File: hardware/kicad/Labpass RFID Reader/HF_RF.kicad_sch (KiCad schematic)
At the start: 22 parts, among them J1 Conn_01x03_Male, U4 MFRC522, Y1 27.12 MHz

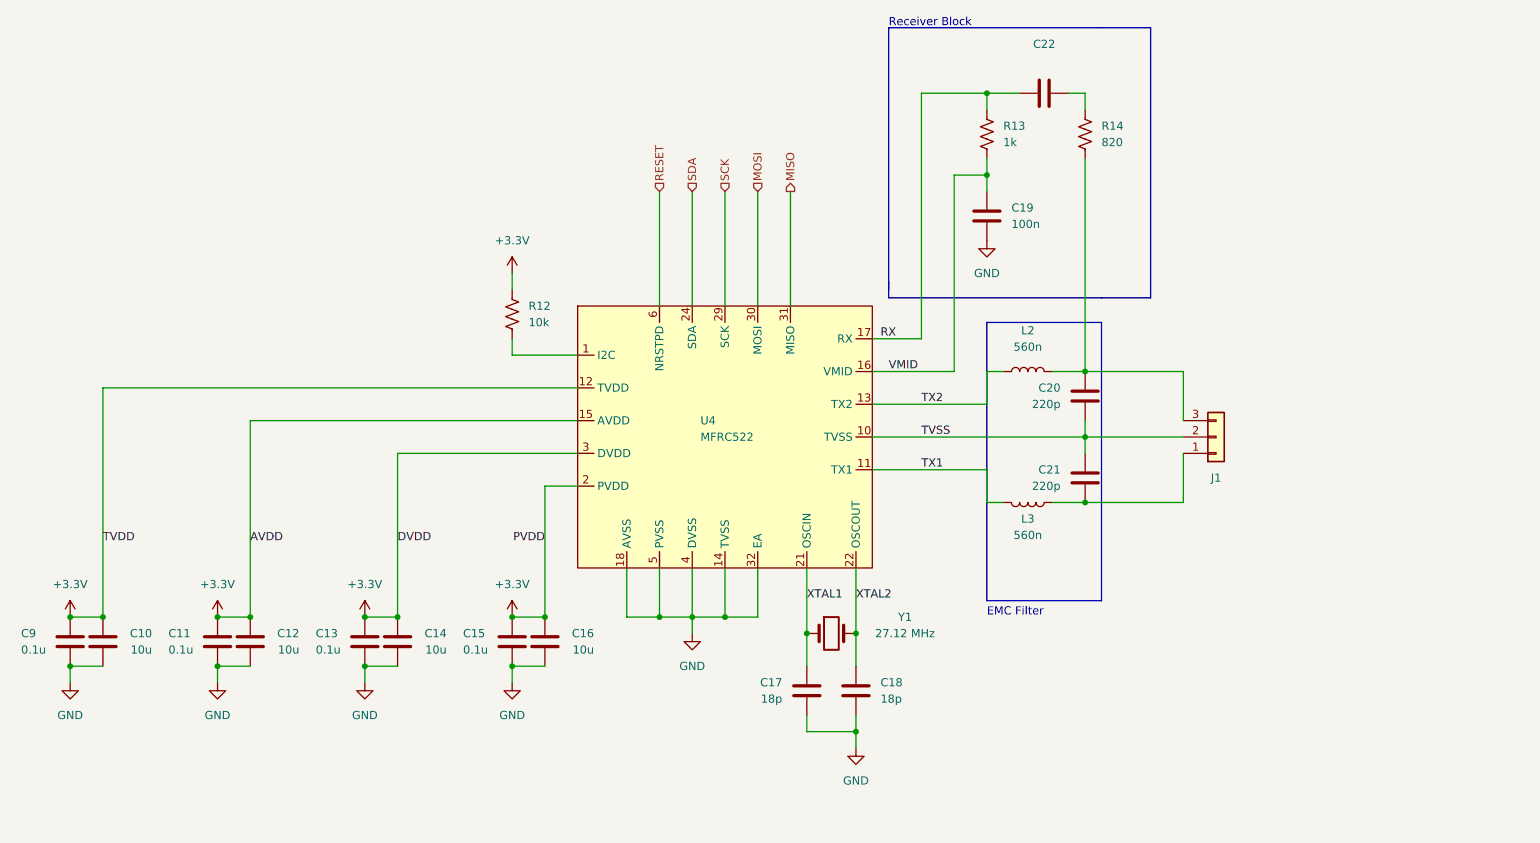
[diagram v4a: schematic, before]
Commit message: Several fixes
* EA and I2C were backwards
* Adding missing Crx into HF receive path
* Better header size and placement
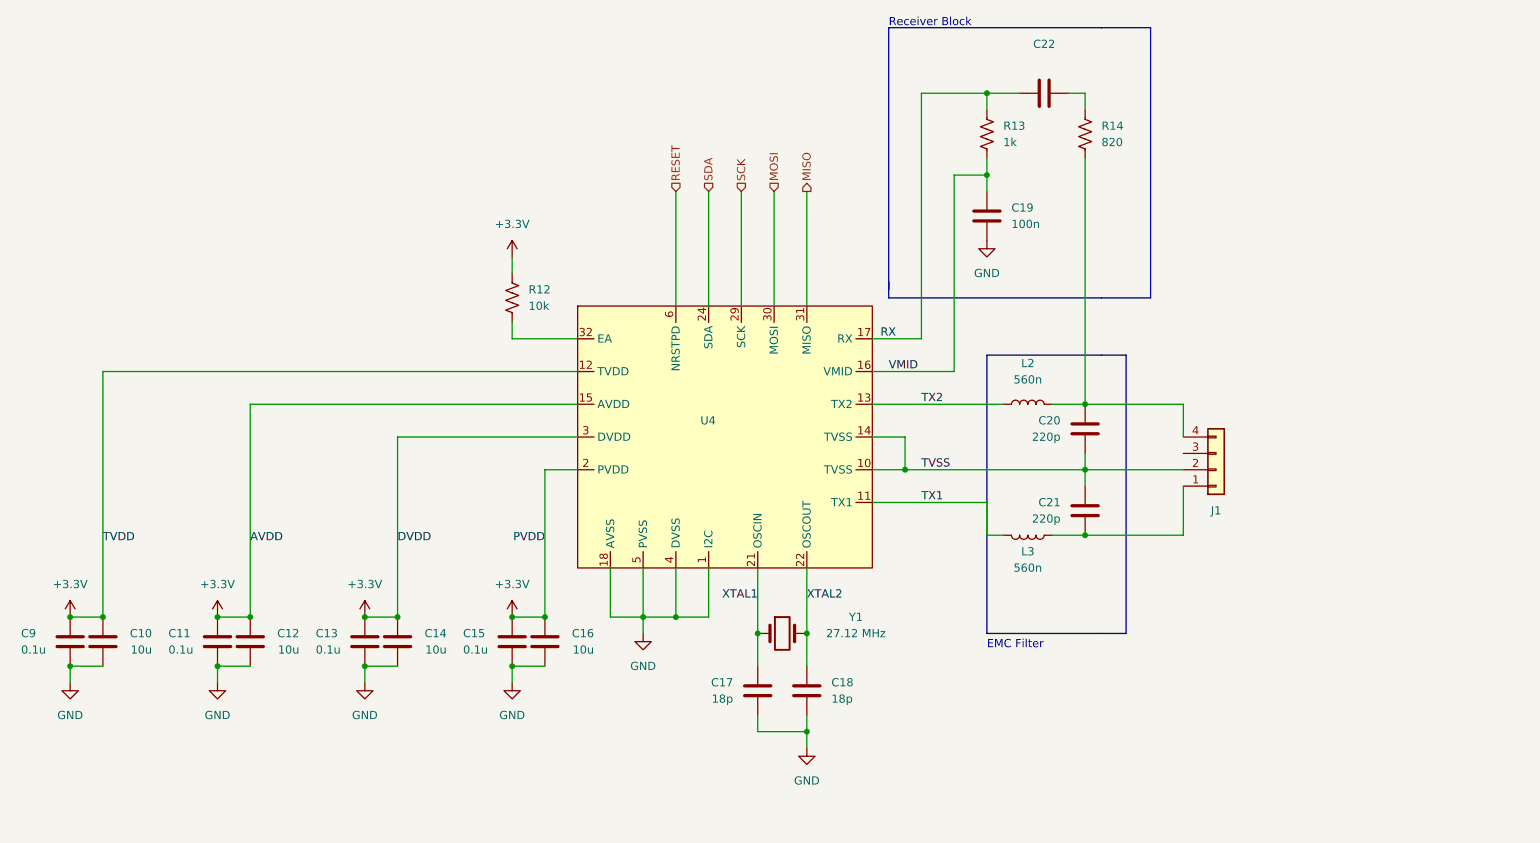
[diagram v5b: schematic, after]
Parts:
- J1: value Conn_01x03_Male -> (none); footprint Connector_PinHeader_2.54mm:PinHeader_1x03_P2.54mm_Vertical_SMD_Pin1Left -> (none); symbol Connector_Generic:Conn_01x03 -> Connector_Generic:Conn_01x04
- U4: value MFRC522 -> (none); footprint Package_QFP:LQFP-32_5x5mm_P0.5mm -> (none)
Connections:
- net GND: now also U4.1 (I2C); no longer U4.14 (TVSS), U4.32 (EA)
- net TVSS: now also U4.14 (TVSS)
- net at R12.2: now also U4.32 (EA); no longer U4.1 (I2C)
- net at C20.2, L2.2, R14.1: now also J1.4 (Pin_4); no longer J1.3 (Pin_3)
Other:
- moved on the sheet: C17, C18, C20, C21, L2, L3, R12, Y1

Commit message: Additional Changes
* remove transistor on LF path and power coil directly
  from ESP TX pin at 3.3V
* add some test points around the HF path
* add some cheap pots on LF for tuning the amplifier bias
  and comparator threshold
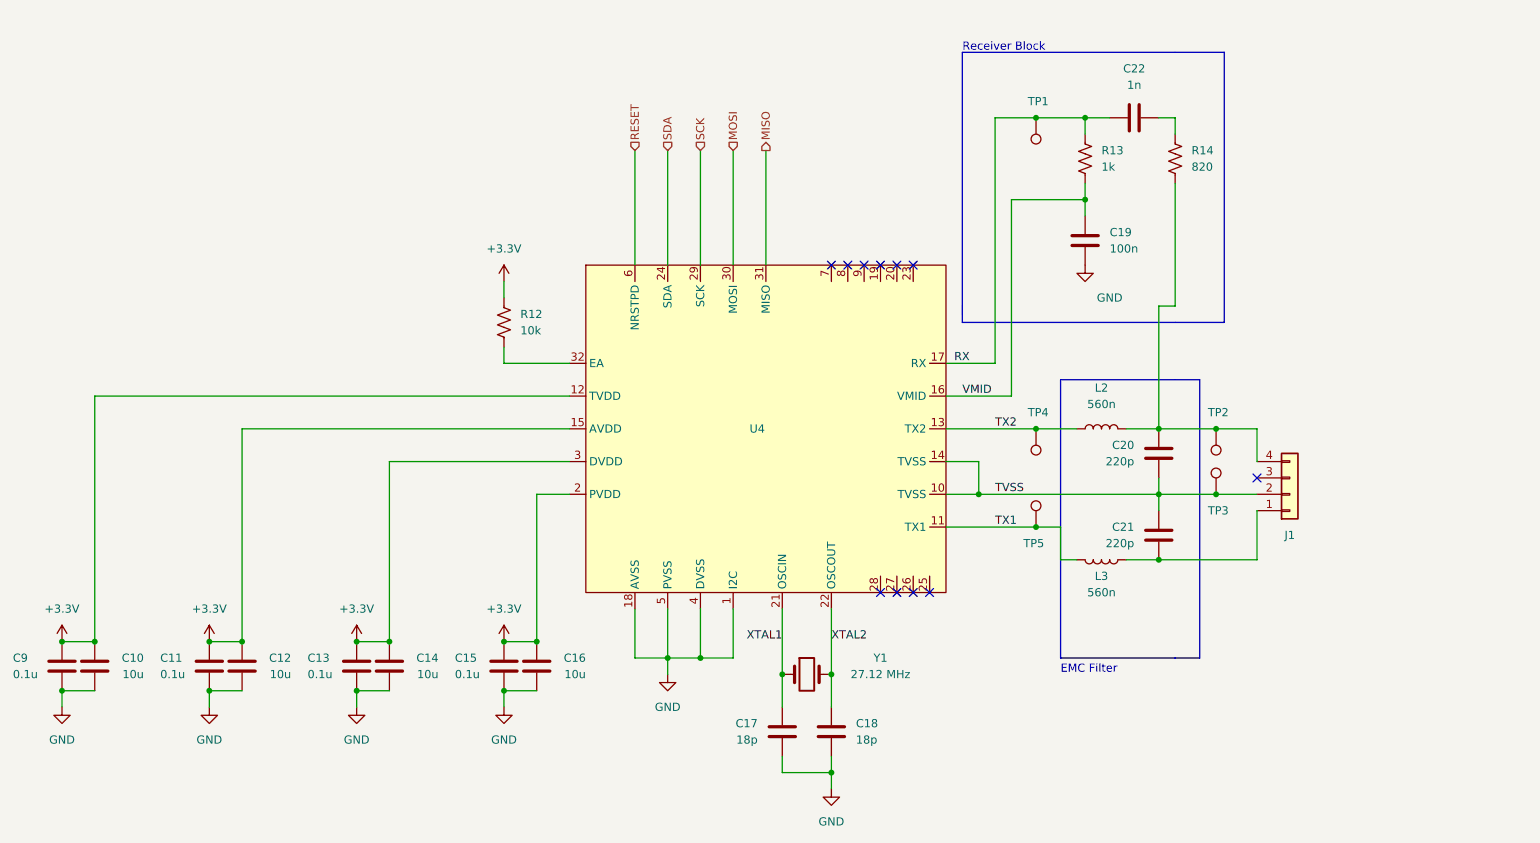
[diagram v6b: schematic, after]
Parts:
- added TP1, TP2, TP3, TP4, TP5: TestPoint, TestPoint:TestPoint_Pad_1.0x1.0mm, symbol Connector:TestPoint
- C22: value (none) -> 1n; footprint (none) -> Capacitor_SMD:C_0603_1608Metric
- J1: value (none) -> Conn_01x03_Male; footprint (none) -> Connector_PinHeader_2.54mm:PinHeader_2x02_P2.54mm_Horizontal
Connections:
- net RX: now also TP1.1
- net TVSS: now also TP3.1
- net TX1: now also TP5.1
- net TX2: now also TP4.1
- net at C20.2, J1.4 (Pin_4), L2.2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: now also TP2.1
- no-connect marks 0 -> 11
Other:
- moved on the sheet: C10, C11, C12, C13, C14, C15, C16, C17, C18, C19, C20, C21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

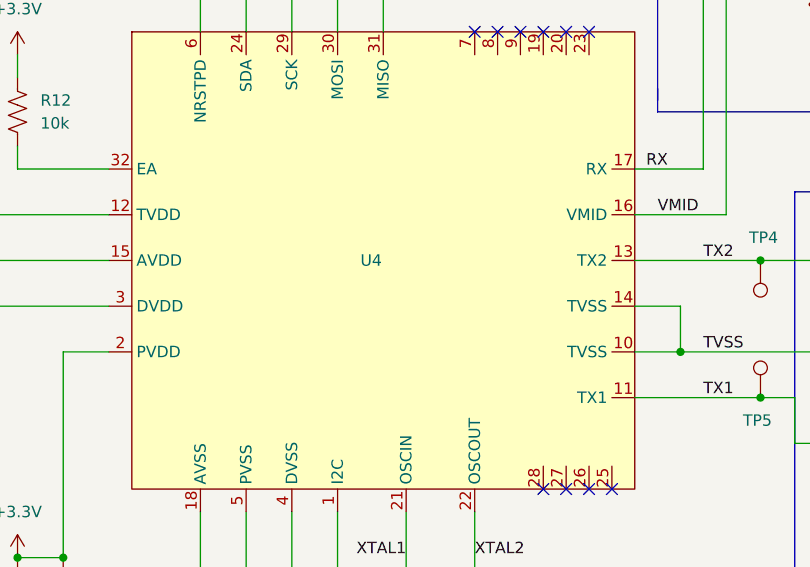
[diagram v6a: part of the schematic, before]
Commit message: Add terminal block for gpio to ext relay
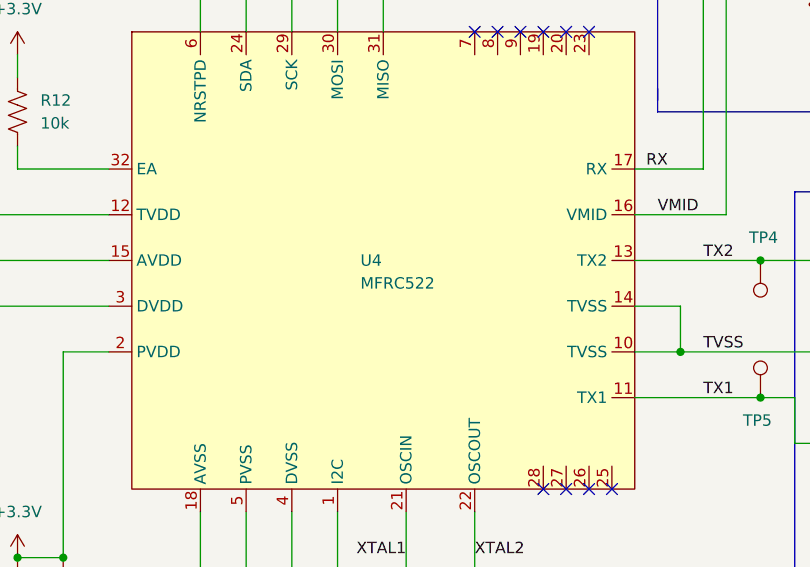
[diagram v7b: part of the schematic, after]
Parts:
- U4: value (none) -> MFRC522; footprint (none) -> Package_QFP:LQFP-32_5x5mm_P0.5mm
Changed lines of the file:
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@@
       (effects (font (size 1.27 1.27)) (justify left))
     )
-    (property "Value" "" (id 1) (at 148.59 95.25 0)
+    (property "Value" "MFRC522" (id 1) (at 148.59 95.25 0)
       (effects (font (size 1.27 1.27)) (justify left))
     )
-    (property "Footprint" "" (id 2) (at 212.09 26.67 0)
+    (property "Footprint" "Package_QFP:LQFP-32_5x5mm_P0.5mm" (id 2) (at 212.09 26.67 0)
       (effects (font (size 1.27 1.27)) hide)
     )

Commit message: tweak incorrect designation for jumper
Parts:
- J1: value Conn_01x03_Male -> (none); footprint Connector_PinHeader_2.54mm:PinHeader_2x02_P2.54mm_Horizontal -> (none)
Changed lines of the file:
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@@
     (in_bom yes) (on_board yes)
     (property "Reference" "J1" (id 0) (at 232.41 109.22 0))
-    (property "Value" "Conn_01x03_Male" (id 1) (at 232.41 96.52 0)
+    (property "Value" "" (id 1) (at 232.41 95.25 0)
       (effects (font (size 1.27 1.27)) hide)
     )
-    (property "Footprint" "Connector_PinHeader_2.54mm:PinHeader_2x02_P2.54mm_Horizontal" (id 2) (at 232.41 102.87 0)
+    (property "Footprint" "" (id 2) (at 232.41 102.87 0)
       (effects (font (size 1.27 1.27)) hide)
     )
